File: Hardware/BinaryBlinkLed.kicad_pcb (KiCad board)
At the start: 2 copper layers, 45 x 20 mm, 14 parts, among them IC1 ATTINY13A-SS, P1 SWITCH, P2 ISCP6, Q1 BC848, Q2 BC848

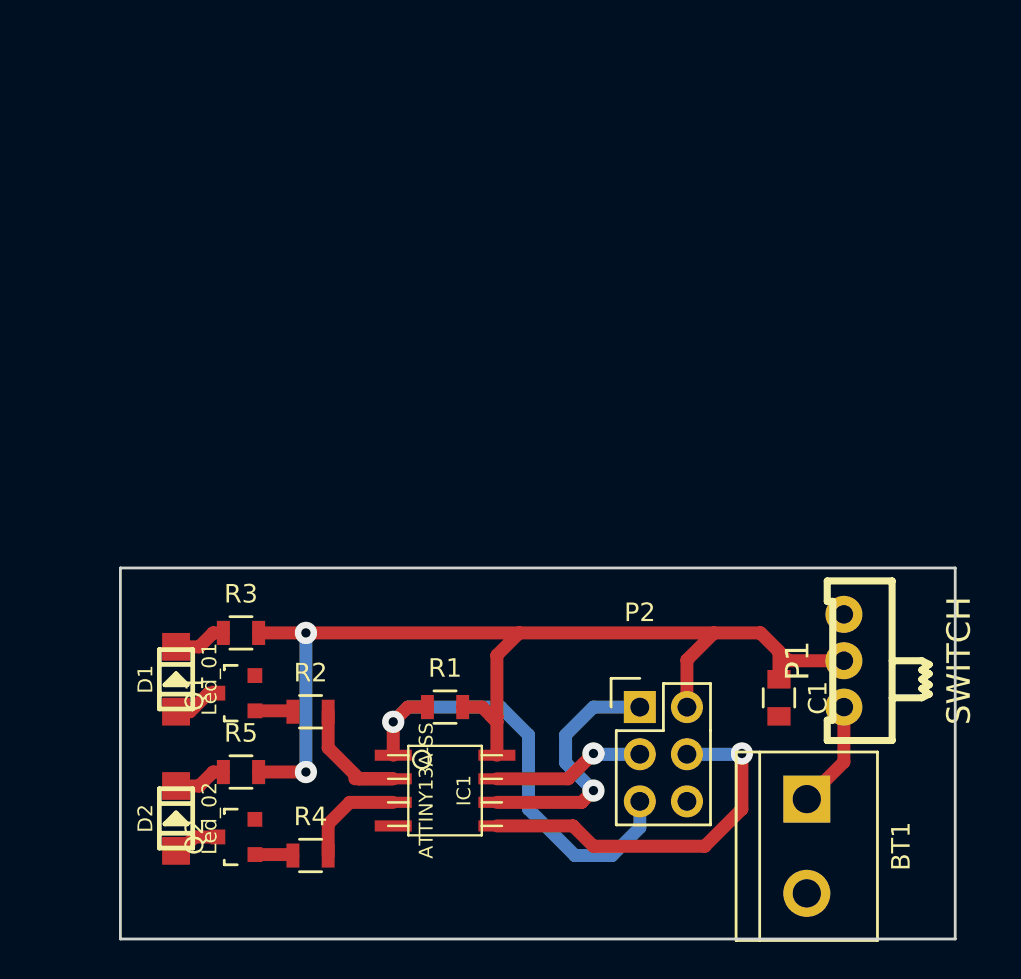
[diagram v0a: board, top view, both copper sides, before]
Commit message: update of schematic, change footprint of switch and battery
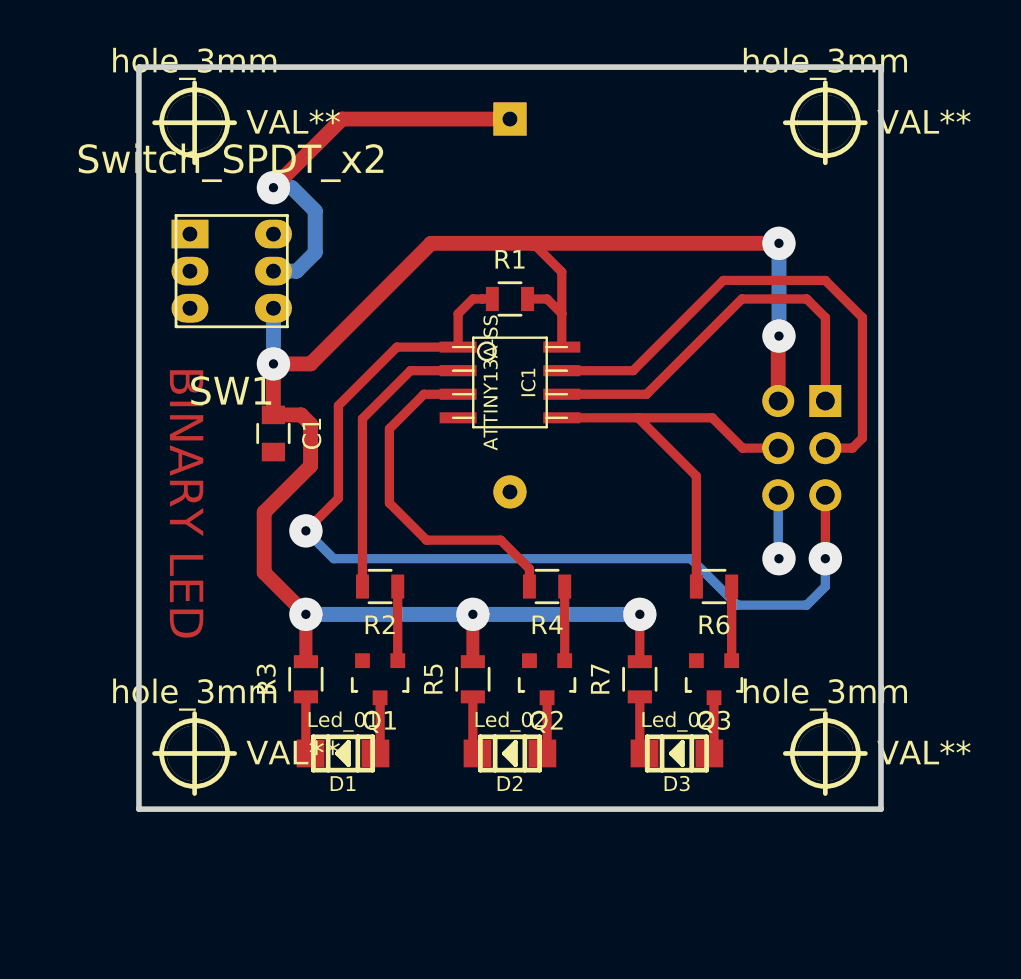
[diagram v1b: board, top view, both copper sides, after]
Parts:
- removed P1: SWITCH, w_switch:switch_mmp122-r
- added D3: Led_02, w_smd_leds:Led_1206, F.Cu at (150.0, 115.0)
- added Q3: BC848, TO_SOT_Packages_SMD:SOT-23, F.Cu at (152.0, 111.0)
- added R6: 10K, Resistors_SMD:R_0805, F.Cu at (152.0, 106.0)
- added R7: 82R, Resistors_SMD:R_0805, F.Cu at (148.0, 111.0)
- added SW1: Switch_SPDT_x2, mc_switch:push_lock_6mm, F.Cu at (126.0, 89.0)
- added hole_3mm: VAL**, w_details:hole_3mm, F.Cu at (158.0, 115.0)
- added hole_3mm: VAL**, w_details:hole_3mm, F.Cu at (158.0, 81.0)
- added hole_3mm: VAL**, w_details:hole_3mm, F.Cu at (124.0, 115.0)
- added hole_3mm: VAL**, w_details:hole_3mm, F.Cu at (124.0, 81.0)
- BT1: value 4.5V -> 3V; footprint Connect:bornier2 -> JG_Misc:JG_BAT; moved to B.Cu
- P2: moved to B.Cu
- R2, R4: value 220R -> 10K
- R3, R5: value 470R -> 82R
- moved BT1 31.4 mm to (141.0, 93.0), turned to 90 degrees
- moved C1 30.8 mm to (128.2, 97.8)
- moved IC1 22.3 mm to (141.0, 95.0)
- moved R1 22.3 mm to (141.0, 90.5)
- moved R4 19.3 mm to (143.0, 106.0), turned to 180 degrees
- moved P2 19.3 mm to (158.0, 96.0), turned to 180 degrees
- moved Q2 18.8 mm to (143.0, 111.0), turned to 180 degrees
- moved D2 18.3 mm to (141.0, 115.0), turned to 180 degrees
- moved R5 13.5 mm to (139.0, 111.0), turned to 90 degrees
- moved D1 9.85 mm to (132.0, 115.0), turned to 180 degrees
- moved Q1 7.79 mm to (134.0, 111.0), turned to 180 degrees
- moved R2 7.72 mm to (134.0, 106.0), turned to 180 degrees
- moved R3 4.30 mm to (130.0, 111.0), turned to 90 degrees
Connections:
- IC1 pad 2: /LED01 -> /LED02
- IC1 pad 3: /LED02 -> /LED03
- R2 pad 2: /LED01 -> /LED02
- R4 pad 2: /LED02 -> /LED03
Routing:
- net +BATT: track 59.7 -> 92.1 mm, vias 2 -> 6
- net /RST: track 25.3 -> 54.2 mm, vias 1 -> 2
- net /SCK: track 8.29 -> 27.8 mm, vias 1 -> 0
- net /LED03: track 0.00 -> 18.4 mm
- net Net-(BT1-Pad1): track 5.79 -> 22.0 mm, vias 0 -> 1
- net /LED02: track 5.69 -> 15.3 mm
- net /LED01: track 8.22 -> 0.00 mm
- net /MISO: track 13.7 -> 21.2 mm, vias 1 -> 0
- net Net-(Q3-Pad1): track 0.00 -> 4.07 mm
- net GND: track 0.00 -> 3.44 mm, vias 0 -> 1
- net Net-(D3-Pad2): track 0.00 -> 3.15 mm
- net Net-(D3-Pad1): track 0.00 -> 3.11 mm
- net /MOSI: track 20.5 -> 22.7 mm, vias 1 -> 0
- net Net-(Q2-Pad1): track 2.07 -> 4.00 mm
- net Net-(Q1-Pad1): track 2.07 -> 4.00 mm
- added copper zone on B.Cu, net GND
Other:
- board size 45 x 20 mm -> 40 x 40 mm
- board text added: "BINARY LED"

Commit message: footprinft resistor changed, walter library used
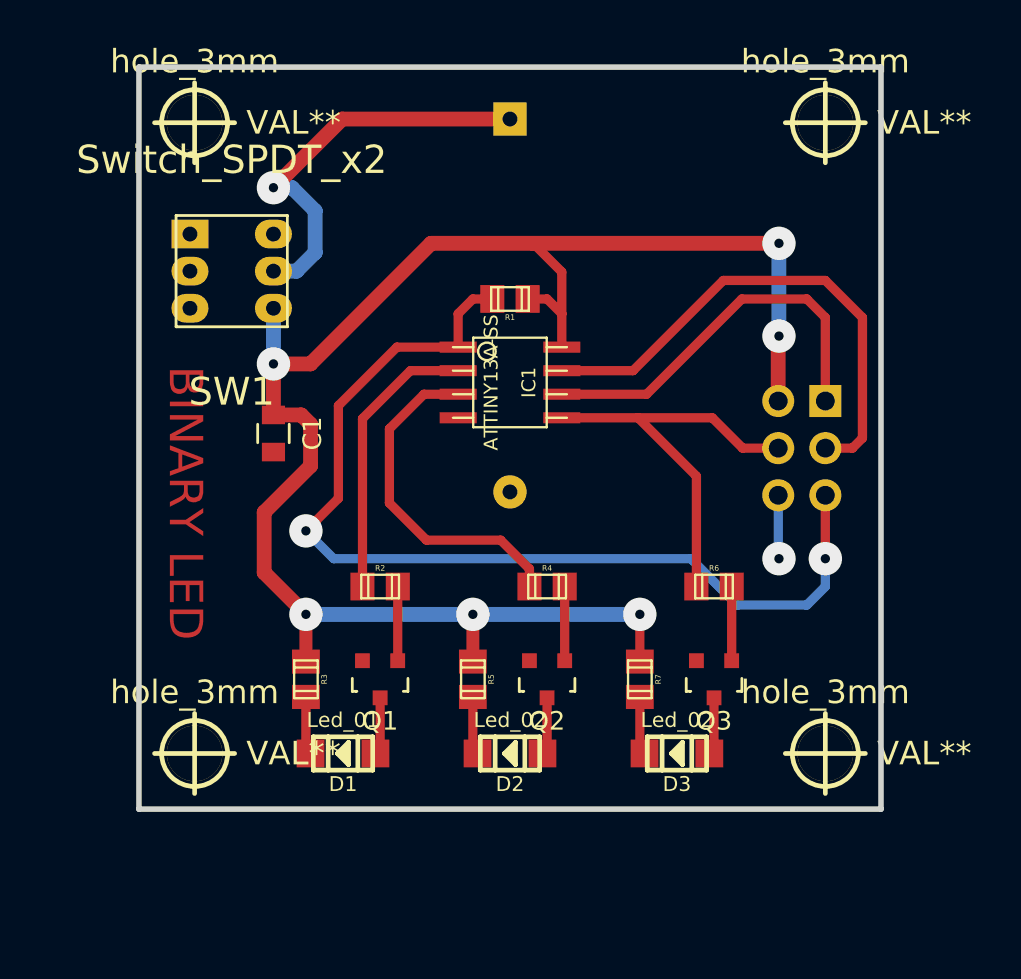
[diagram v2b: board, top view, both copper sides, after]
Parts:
- R1, R2, R3, R4, R5, R6, R7: footprint Resistors_SMD:R_0805 -> w_smd_resistors:r_0805
- turned R1 to 180 degrees
- turned R2 to 0 degrees
- turned R3 to 270 degrees
- turned R4 to 0 degrees
- turned R5 to 270 degrees
- turned R6 to 0 degrees
- turned R7 to 270 degrees
